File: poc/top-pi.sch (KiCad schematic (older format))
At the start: 118 parts

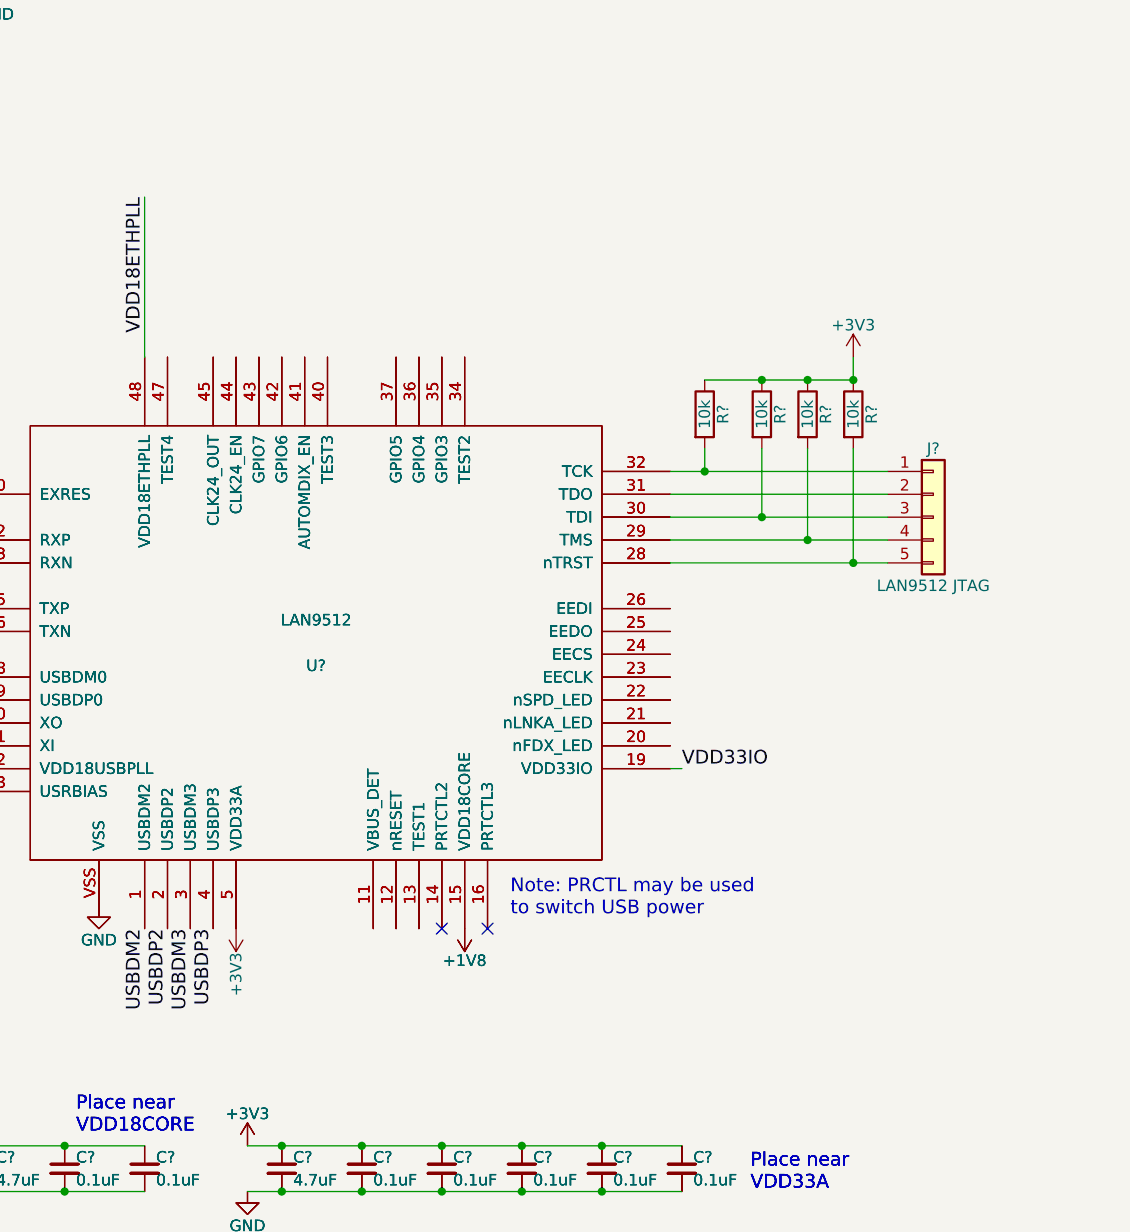
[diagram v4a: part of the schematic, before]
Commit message: LAN9512 Misc. Pins (LEDs, GPIO, etc)
Of note, we're enabling Auto-MDIX; strictly, this shouldn't be
necessary, but I feel we're better safe than sorry.
I've left a note to route a GND connect nearby so we can switch
it off if need be.
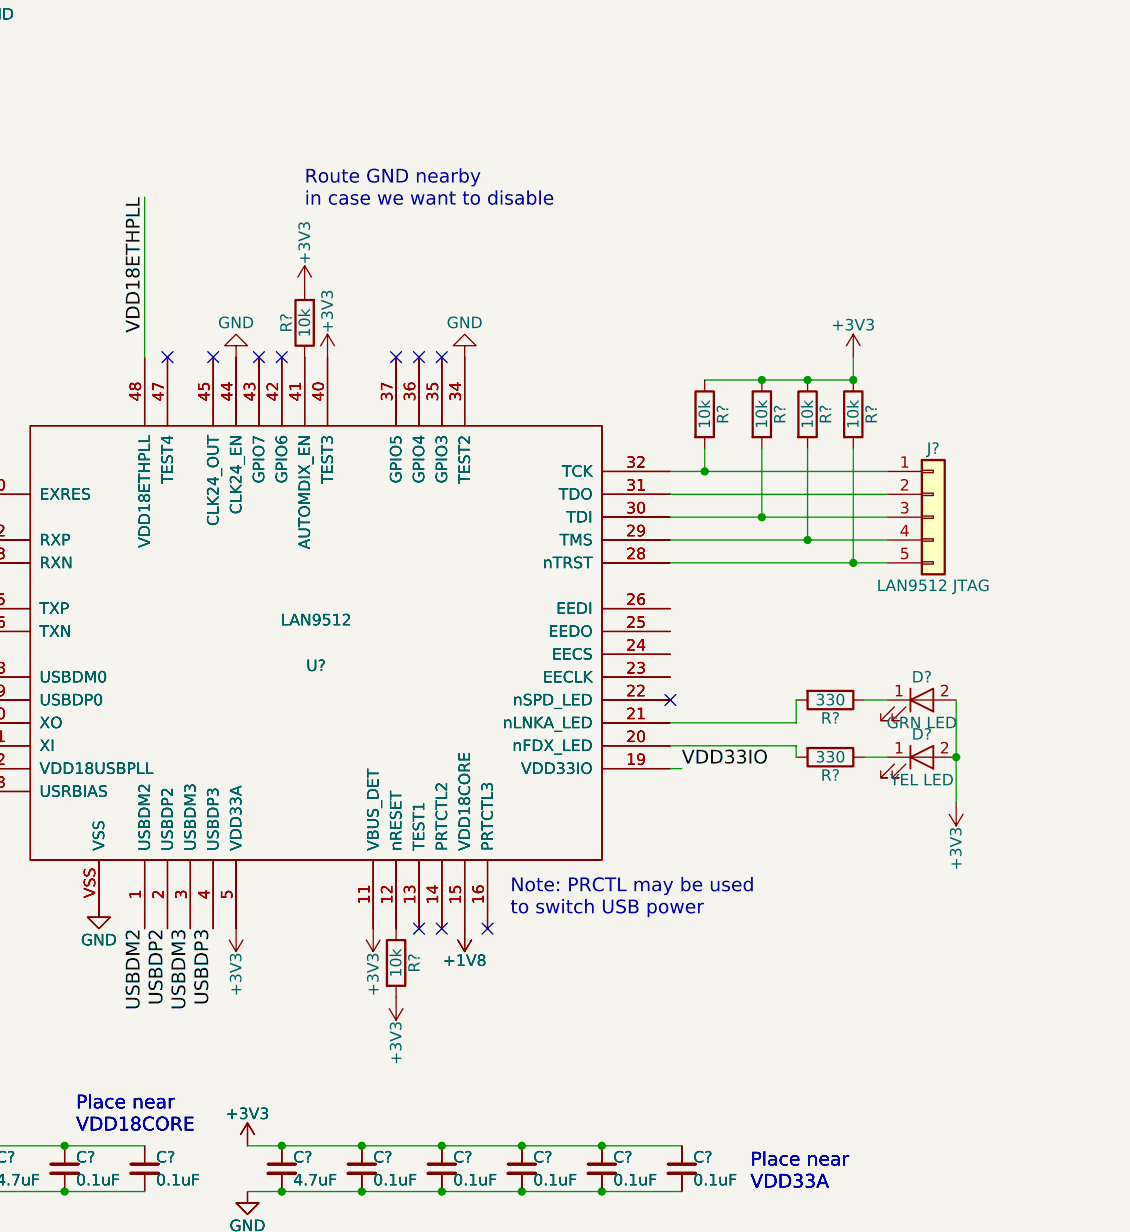
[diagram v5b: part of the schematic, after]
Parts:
- added D?: GRN LED, symbol LED
- added D?: YEL LED, symbol LED
- added R? (x2): 10k, symbol R
- added R? (x2): 330, symbol R
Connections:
- net +3V3: now also U?.11 (VBUS_DET), U?.11 (VBUS_DET), U?.40 (TEST3), U?.40 (TEST3), D?.2 (A), D?.2 (A), R?.2, R?.2
- net GND: now also U?.34 (TEST2), U?.34 (TEST2), U?.44 (CLK24_EN), U?.44 (CLK24_EN)
- net at U?.12 (nRESET), U?.12 (nRESET): now also R?.1
- net at U?.20 (nFDX_LED), U?.20 (nFDX_LED): now also R?.2
- net at U?.21 (nLNKA_LED), U?.21 (nLNKA_LED): now also R?.2
- net at U?.41 (AUTOMDIX_EN), U?.41 (AUTOMDIX_EN): now also R?.1
- new net: D?.1 (K), R?.1 (x2)
- no-connect marks 2 -> 11
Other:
- note added: "Route GND nearby\nin case we want to disable"
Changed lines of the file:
@@
 	6850 11250 6850 11150
 Connection ~ 6850 11250
+$Comp
+L R R?
+U 1 1 5A56A57A
+P 4850 13800
+F 0 "R?" V 4930 13800 50  0000 C CNN
+F 1 "10k" V 4850 13800 50  0000 C CNN
+F 2 "" V 4780 13800 50  0001 C CNN
+F 3 "" H 4850 13800 50  0001 C CNN
+	1    4850 13800
+	1    0    0    -1
+$EndComp
+$Comp
+L +3V3 #PWR?
+U 1 1 5A56A806
+P 4850 13950
+F 0 "#PWR?" H 4850 13800 50  0001 C CNN
+F 1 "+3V3" V 4850 14150 50  0000 C CNN
+F 2 "" H 4850 13950 50  0001 C CNN
+F 3 "" H 4850 13950 50  0001 C CNN
+	1    4850 13950
+	-1   0    0    1
+$EndComp
+NoConn ~ 6050 12650
+$Comp
+L R R?
+U 1 1 5A56CD7E
+P 6750 12900
+F 0 "R?" V 6830 12900 50  0000 C CNN
+F 1 "330" V 6750 12900 50  0000 C CNN
+F 2 "" V 6680 12900 50  0001 C CNN
+F 3 "" H 6750 12900 50  0001 C CNN
+	1    6750 12900
+	0    1    1    0
+$EndComp
+$Comp
+L R R?
+U 1 1 5A56D3D8
+P 6750 12650
+F 0 "R?" V 6830 12650 50  0000 C CNN
+F 1 "330" V 6750 12650 50  0000 C CNN
+F 2 "" V 6680 12650 50  0001 C CNN
+F 3 "" H 6750 12650 50  0001 C CNN
+	1    6750 12650
+	0    1    1    0
+$EndComp
+$Comp
+L LED D?
+U 1 1 5A56D8C6
+P 7150 12650
+F 0 "D?" H 7150 12750 50  0000 C CNN
+F 1 "GRN LED" H 7150 12550 50  0000 C CNN
+F 2 "" H 7150 12650 50  0001 C CNN
+F 3 "" H 7150 12650 50  0001 C CNN
+	1    7150 12650
+	1    0    0    -1
+$EndComp
+$Comp
+L LED D?
+U 1 1 5A56DB5B
+P 7150 12900
+F 0 "D?" H 7150 13000 50  0000 C CNN
+F 1 "YEL LED" H 7150 12800 50  0000 C CNN
+F 2 "" H 7150 12900 50  0001 C CNN
+F 3 "" H 7150 12900 50  0001 C CNN
+	1    7150 12900
+	1    0    0    -1
+$EndComp
+$Comp
+L +3V3 #PWR?
+U 1 1 5A56DE7D
+P 7300 13100
+F 0 "#PWR?" H 7300 12950 50  0001 C CNN
+F 1 "+3V3" V 7300 13300 50  0000 C CNN
+F 2 "" H 7300 13100 50  0001 C CNN
+F 3 "" H 7300 13100 50  0001 C CNN
+	1    7300 13100
+	-1   0    0    1
+$EndComp
+Wire Wire Line
+	7300 12650 7300 13100
+Connection ~ 7300 12900
+Wire Wire Line
+	7000 12650 6900 12650
+Wire Wire Line
+	6900 12900 7000 12900
+Wire Wire Line
+	6600 12900 6600 12850
+Wire Wire Line
+	6600 12850 6050 12850
+Wire Wire Line
+	6050 12750 6600 12750
+Wire Wire Line
+	6600 12750 6600 12650
+NoConn ~ 5050 11150
+NoConn ~ 4950 11150
+NoConn ~ 4850 11150
+NoConn ~ 4350 11150
+NoConn ~ 4250 11150
+$Comp
+L +3V3 #PWR?
+U 1 1 5A574591
+P 4750 13650
+F 0 "#PWR?" H 4750 13500 50  0001 C CNN
+F 1 "+3V3" V 4750 13850 50  0000 C CNN
+F 2 "" H 4750 13650 50  0001 C CNN
+F 3 "" H 4750 13650 50  0001 C CNN
+	1    4750 13650
+	-1   0    0    1
+$EndComp
+$Comp
+L R R?
+U 1 1 5A577F32
+P 4450 11000
+F 0 "R?" V 4530 11000 50  0000 C CNN
+F 1 "10k" V 4450 11000 50  0000 C CNN
+F 2 "" V 4380 11000 50  0001 C CNN
+F 3 "" H 4450 11000 50  0001 C CNN
+	1    4450 11000
+	-1   0    0    1
+$EndComp
+$Comp
+L +3V3 #PWR?
+U 1 1 5A577F38
+P 4450 10850
+F 0 "#PWR?" H 4450 10700 50  0001 C CNN
+F 1 "+3V3" V 4450 11050 50  0000 C CNN
+F 2 "" H 4450 10850 50  0001 C CNN
+F 3 "" H 4450 10850 50  0001 C CNN
+	1    4450 10850
+	1    0    0    -1
+$EndComp
+NoConn ~ 4950 13650
+$Comp
+L GND #PWR?
+U 1 1 5A578E0F
+P 5150 11150
+F 0 "#PWR?" H 5150 10900 50  0001 C CNN
+F 1 "GND" H 5150 11000 50  0000 C CNN
+F 2 "" H 5150 11150 50  0001 C CNN
+F 3 "" H 5150 11150 50  0001 C CNN
+	1    5150 11150
+	-1   0    0    1
+$EndComp
+$Comp
+L +3V3 #PWR?
+U 1 1 5A57957E
+P 4550 11150
+F 0 "#PWR?" H 4550 11000 50  0001 C CNN
+F 1 "+3V3" V 4550 11350 50  0000 C CNN
+F 2 "" H 4550 11150 50  0001 C CNN
+F 3 "" H 4550 11150 50  0001 C CNN
+	1    4550 11150
+	1    0    0    -1
+$EndComp
+NoConn ~ 3850 11150
+NoConn ~ 4050 11150
+$Comp
+L GND #PWR?
+U 1 1 5A579D72
+P 4150 11150
+F 0 "#PWR?" H 4150 10900 50  0001 C CNN
+F 1 "GND" H 4150 11000 50  0000 C CNN
+F 2 "" H 4150 11150 50  0001 C CNN
+F 3 "" H 4150 11150 50  0001 C CNN
+	1    4150 11150
+	-1   0    0    1
+$EndComp
+Text Notes 4450 10500 0    60   ~ 0
+Route GND nearby\nin case we want to disable
 $EndSCHEMATC

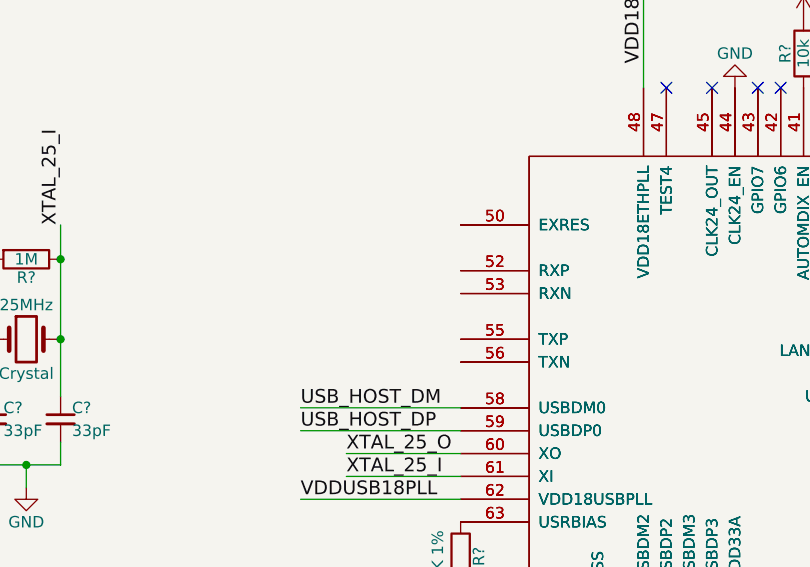
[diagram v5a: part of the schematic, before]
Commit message: LAN9512 Ethernet wiring
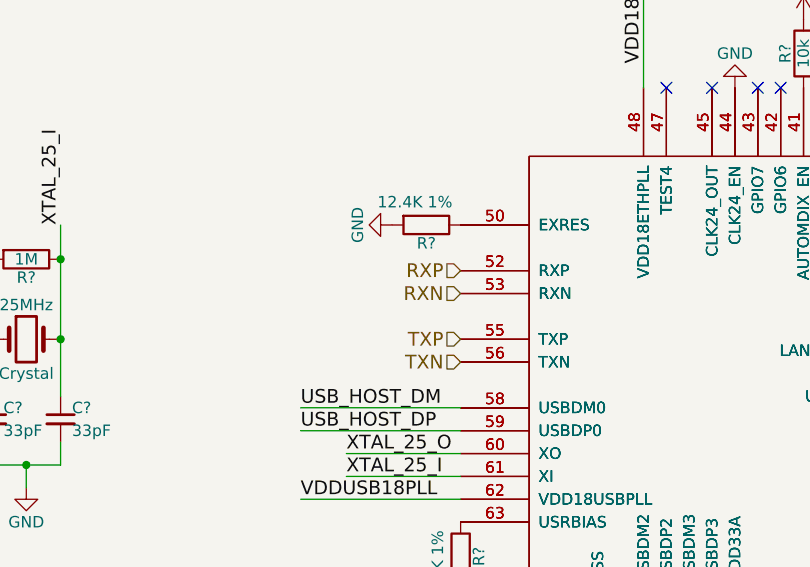
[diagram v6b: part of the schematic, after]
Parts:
- added R?: 12.4K 1%, symbol R
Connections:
- net GND: now also R?.2
- net at U?.50 (EXRES), U?.50 (EXRES): now also R?.1
- net RXP: now reaches U?.52 (RXP), U?.52 (RXP)
- net RXN: now reaches U?.53 (RXN), U?.53 (RXN)
- net TXP: now reaches U?.55 (TXP), U?.55 (TXP)
- net TXN: now reaches U?.56 (TXN), U?.56 (TXN)
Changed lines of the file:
@@
 Text Notes 4450 10500 0    60   ~ 0
 Route GND nearby\nin case we want to disable
+$Comp
+L R R?
+U 1 1 5A57D5CF
+P 2800 11750
+F 0 "R?" V 2880 11750 50  0000 C CNN
+F 1 "12.4K 1%" V 2700 11700 50  0000 C CNN
+F 2 "" V 2730 11750 50  0001 C CNN
+F 3 "" H 2800 11750 50  0001 C CNN
+	1    2800 11750
+	0    1    1    0
+$EndComp
+$Comp
+L GND #PWR?
+U 1 1 5A57D886
+P 2650 11750
+F 0 "#PWR?" H 2650 11500 50  0001 C CNN
+F 1 "GND" H 2650 11600 50  0000 C CNN
+F 2 "" H 2650 11750 50  0001 C CNN
+F 3 "" H 2650 11750 50  0001 C CNN
+	1    2650 11750
+	0    1    1    0
+$EndComp
+Text HLabel 2950 11950 0    60   Input ~ 0
+RXP
+Text HLabel 2950 12050 0    60   Input ~ 0
+RXN
+Text HLabel 2950 12250 0    60   Input ~ 0
+TXP
+Text HLabel 2950 12350 0    60   Input ~ 0
+TXN
 $EndSCHEMATC

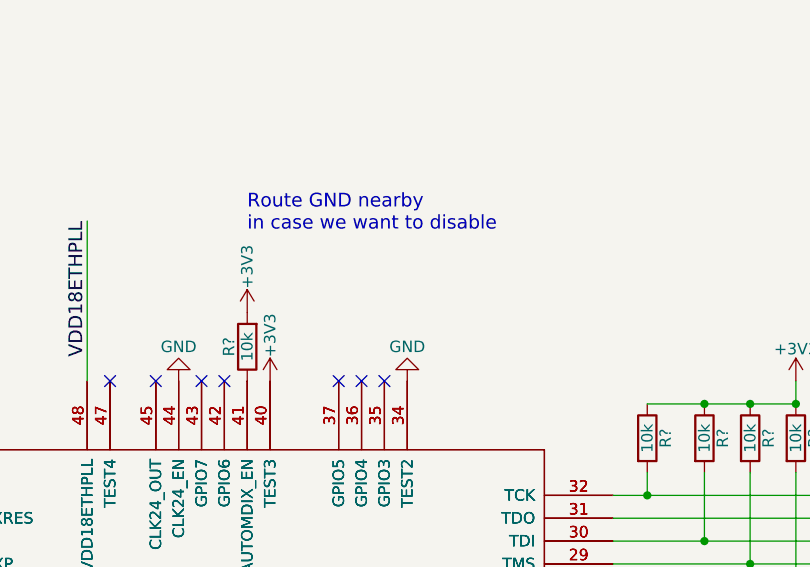
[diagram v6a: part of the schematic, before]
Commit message: Disable Auto-MDIX instead
On second thought, auto-MDIX probably just complicates things.
The pin next to it is tied to 3v3, so if we really need it we can bodge
in a pull-up resistor relatively easily.
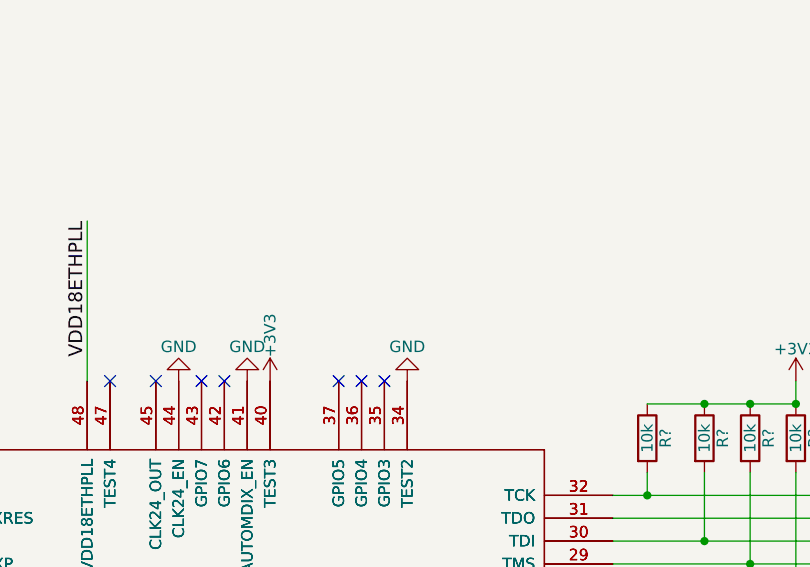
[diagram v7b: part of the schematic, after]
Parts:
- removed R?: 10k, symbol R
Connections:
- net GND: now also U?.41 (AUTOMDIX_EN), U?.41 (AUTOMDIX_EN)
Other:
- note removed: "Route GND nearby\nin case we want to disable"
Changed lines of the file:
@@
 	-1   0    0    1
-$EndComp
-$Comp
-L R R?
-U 1 1 5A577F32
-P 4450 11000
-F 0 "R?" V 4530 11000 50  0000 C CNN
-F 1 "10k" V 4450 11000 50  0000 C CNN
-F 2 "" V 4380 11000 50  0001 C CNN
-F 3 "" H 4450 11000 50  0001 C CNN
-	1    4450 11000
-	-1   0    0    1
-$EndComp
-$Comp
-L +3V3 #PWR?
-U 1 1 5A577F38
-P 4450 10850
-F 0 "#PWR?" H 4450 10700 50  0001 C CNN
-F 1 "+3V3" V 4450 11050 50  0000 C CNN
-F 2 "" H 4450 10850 50  0001 C CNN
-F 3 "" H 4450 10850 50  0001 C CNN
-	1    4450 10850
-	1    0    0    -1
 $EndComp
 NoConn ~ 4950 13650
@@
 	-1   0    0    1
 $EndComp
-Text Notes 4450 10500 0    60   ~ 0
-Route GND nearby\nin case we want to disable
 $Comp
 L R R?
@@
 Text HLabel 2950 12350 0    60   Input ~ 0
 TXN
+$Comp
+L GND #PWR?
+U 1 1 5A537556
+P 4450 11150
+F 0 "#PWR?" H 4450 10900 50  0001 C CNN
+F 1 "GND" H 4450 11000 50  0000 C CNN
+F 2 "" H 4450 11150 50  0001 C CNN
+F 3 "" H 4450 11150 50  0001 C CNN
+	1    4450 11150
+	-1   0    0    1
+$EndComp
 $EndSCHEMATC
